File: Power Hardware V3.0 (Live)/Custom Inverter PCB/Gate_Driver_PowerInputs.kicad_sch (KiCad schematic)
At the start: 22 parts, among them J1 1714971, J2 1714971, J3 1714968, J7 1714971, J8 1714971, K2 1-1393210-3, U1 DRV8300DIPWR

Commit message: Datasheets into components
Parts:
- CR4: Part Number (none) -> LD1085D2M33R
- K2: Part Number (none) -> 1-1393210-3
- U1: Part Number (none) -> DRV8300DIPWR
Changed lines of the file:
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@@
 			)
 		)
-		(property "Datasheet" "DRV8300DIPWR"
+		(property "Datasheet" "https://www.ti.com/lit/ds/symlink/drv8300.pdf"
 			(at 173.99 30.48 0)
 			(effects
@@
 			)
 		)
-		(property "Description" ""
+		(property "Description" "IC GATE DRV HI/LOW SIDE 20HTSSOP"
 			(at 173.99 30.48 0)
 			(effects
@@
 			)
 		)
-		(property "Part Number" ""
+		(property "Part Number" "DRV8300DIPWR"
 			(at 173.99 30.48 0)
 			(effects
@@
 			)
 		)
-		(property "Datasheet" "LD1085D2M33R"
+		(property "Datasheet" "https://www.st.com/content/ccc/resource/technical/document/datasheet/d3/84/d5/f6/3c/23/40/7b/CD00001883.pdf/files/CD00001883.pdf/jcr:content/translations/en.CD00001883.pdf"
 			(at 133.35 147.32 0)
 			(effects
@@
 			)
 		)
-		(property "Description" ""
+		(property "Description" "IC REG LINEAR 3.3V 3A D2PAK-3"
+			(at 133.35 147.32 0)
+			(effects
+				(font
+					(size 1.27 1.27)
+				)
+				(hide yes)
+			)
+		)
+		(property "Part Number" "LD1085D2M33R"
 			(at 133.35 147.32 0)
 			(effects
@@
 			)
 		)
-		(property "Datasheet" ""
+		(property "Datasheet" "https://www.te.com/en/product-1-1393210-3.datasheet.pdf"
 			(at 123.19 67.31 0)
 			(effects
@@
 			)
 		)
-		(property "Description" ""
+		(property "Description" "General Purpose Power Relay, DC, Monostable, 1 Form A SPST-NO, 30 A Contact Rating, 12 VDC Coil Voltage, Potter & Brumfield T9A"
 			(at 123.19 67.31 0)
 			(effects
@@
 			)
 		)
-		(property "Part Number" ""
+		(property "Part Number" "1-1393210-3"
 			(at 123.19 67.31 0)
 			(effects

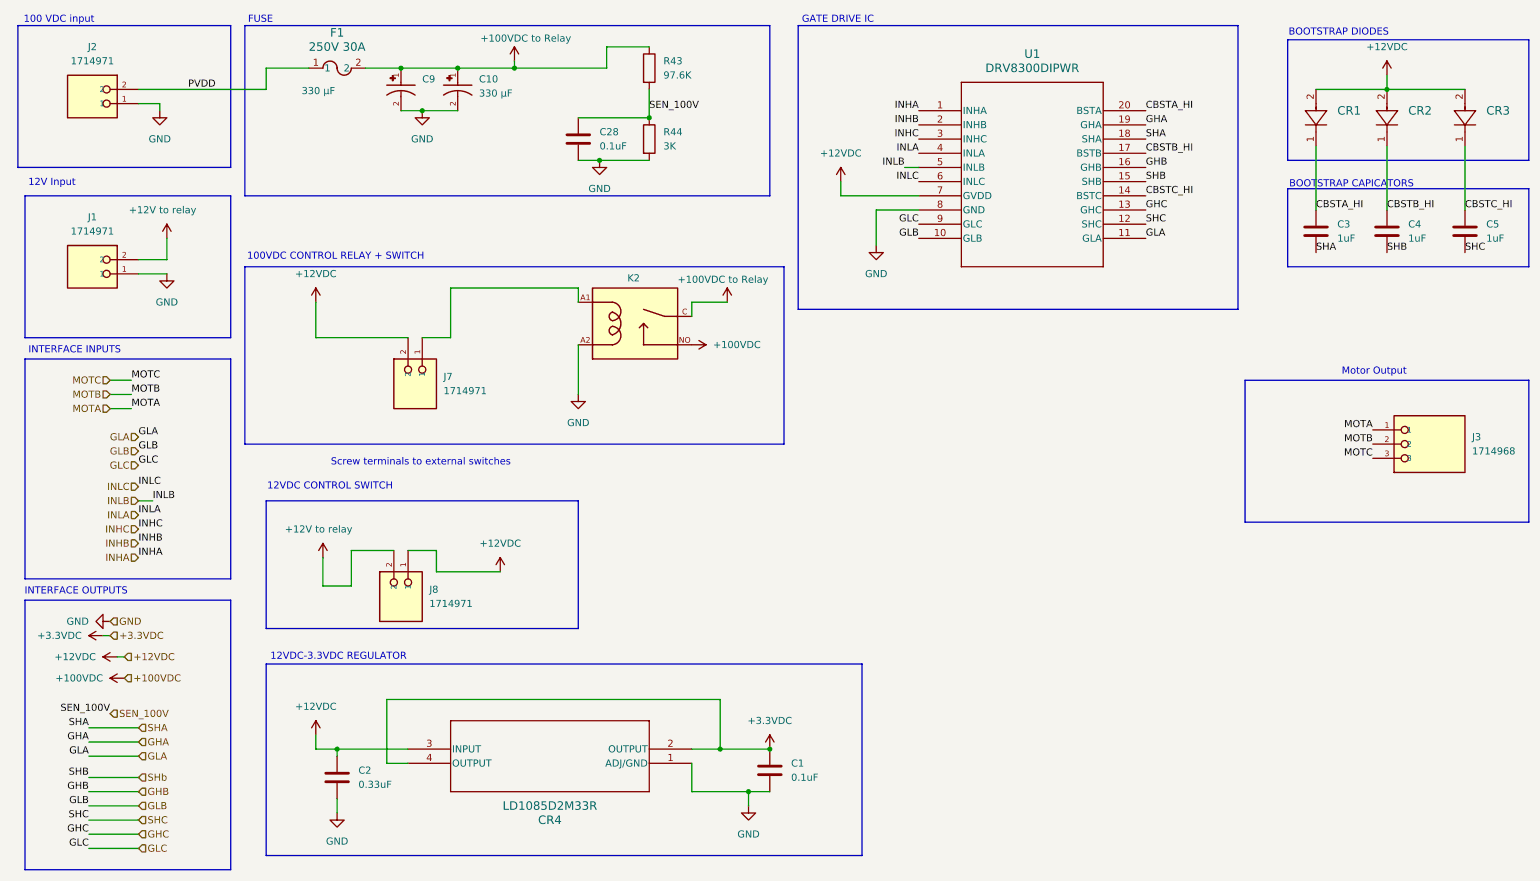
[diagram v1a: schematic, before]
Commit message: Added 100-12 and 12-5 regulators added fan headers
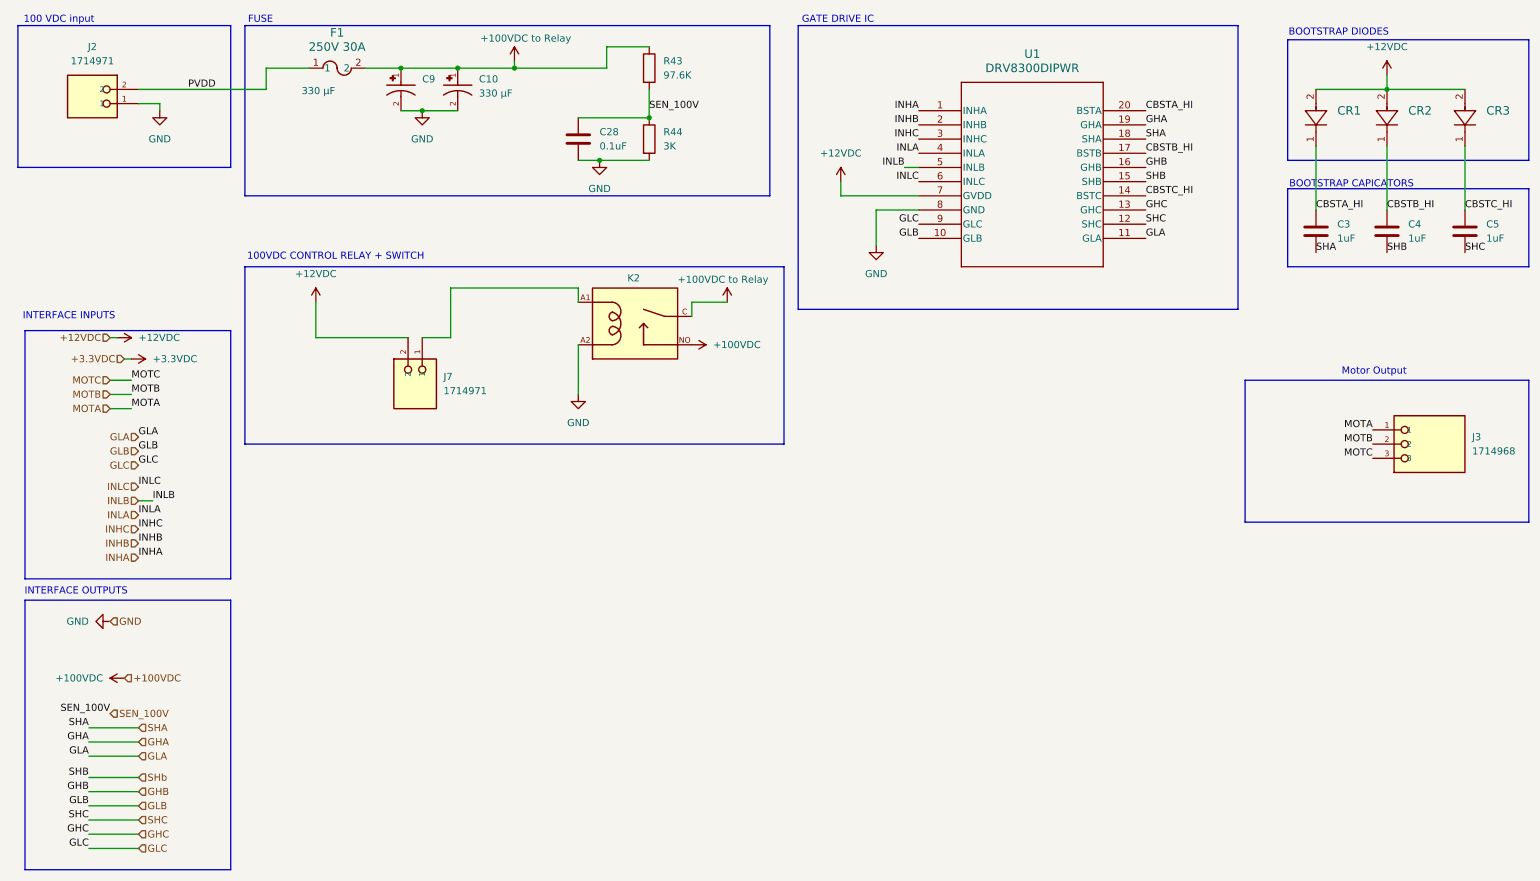
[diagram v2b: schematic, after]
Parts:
- removed C1: 0.1uF, Capacitor_SMD:C_0805_2012Metric, symbol Device:C
- removed C2: 0.33uF, Capacitor_SMD:C_0805_2012Metric, symbol Device:C
- removed CR4: LD1085D2M33R, LD1085D2M33R:D2PAK&slash_A_STM, symbol 3.3V Regulator:LD1085D2M33R
- removed J1, J8: 1714971, 1714971:PHOENIX_1714971, symbol 1714971:1714971
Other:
- note removed: "12V Input"
- note removed: "12VDC CONTROL SWITCH"
- note removed: "12VDC-3.3VDC REGULATOR"
- note removed: "Screw terminals to external switches"

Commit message: Fixes
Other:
- moved on the sheet: J7, K2

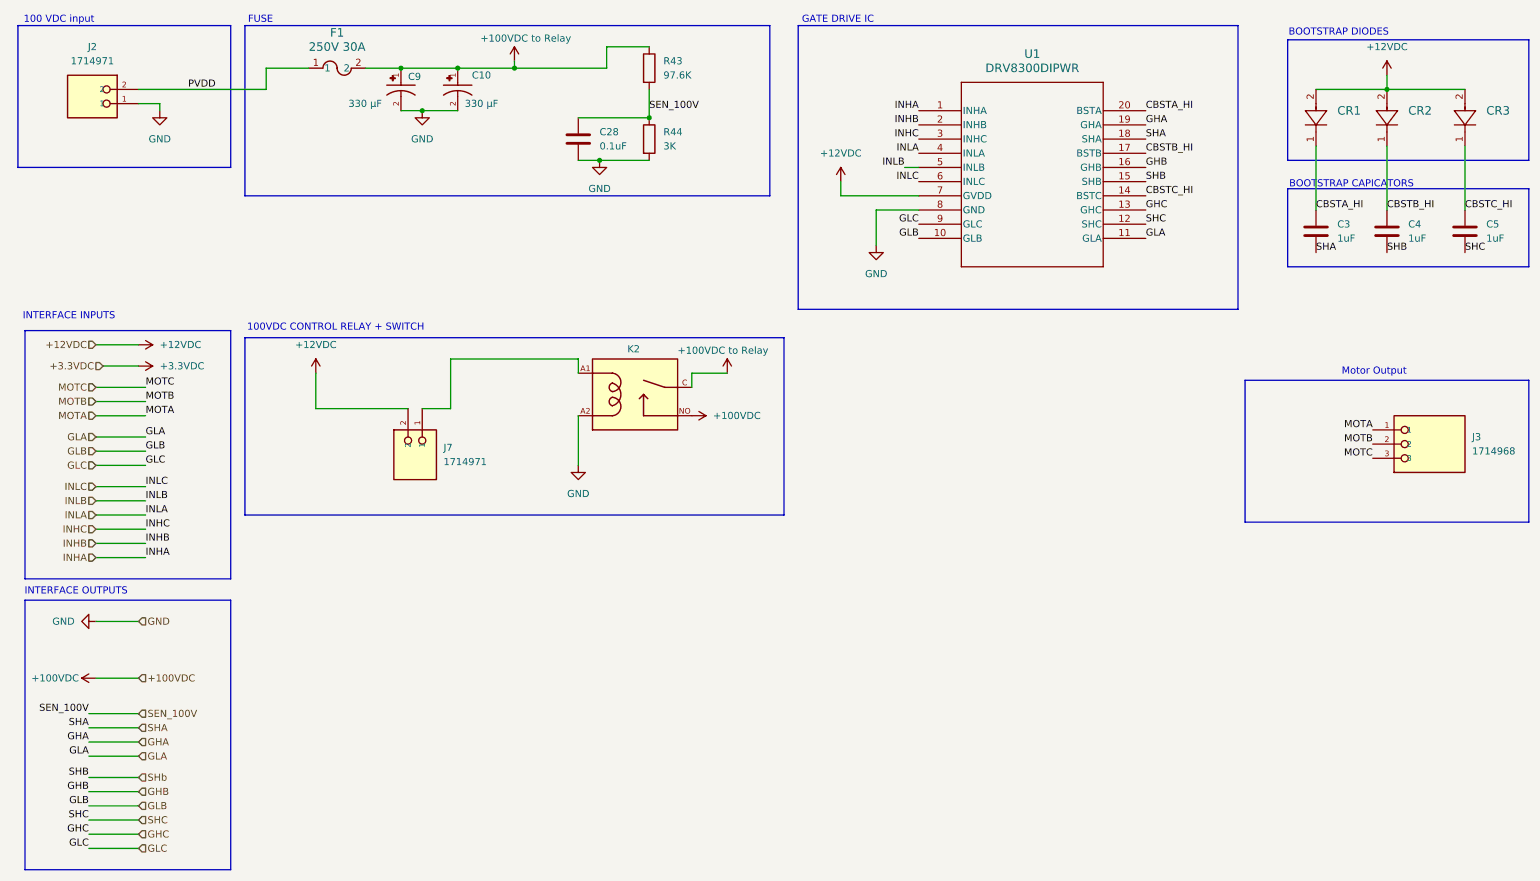
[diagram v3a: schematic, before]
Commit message: PCB V3 changes
-HV outputs and inputs changed to screw terminals for lugs
- Fuses changes to 50A
- ADC pin for temp sense along with the temp sensing circuit
- Added more pins to motor encoder term for temp sense
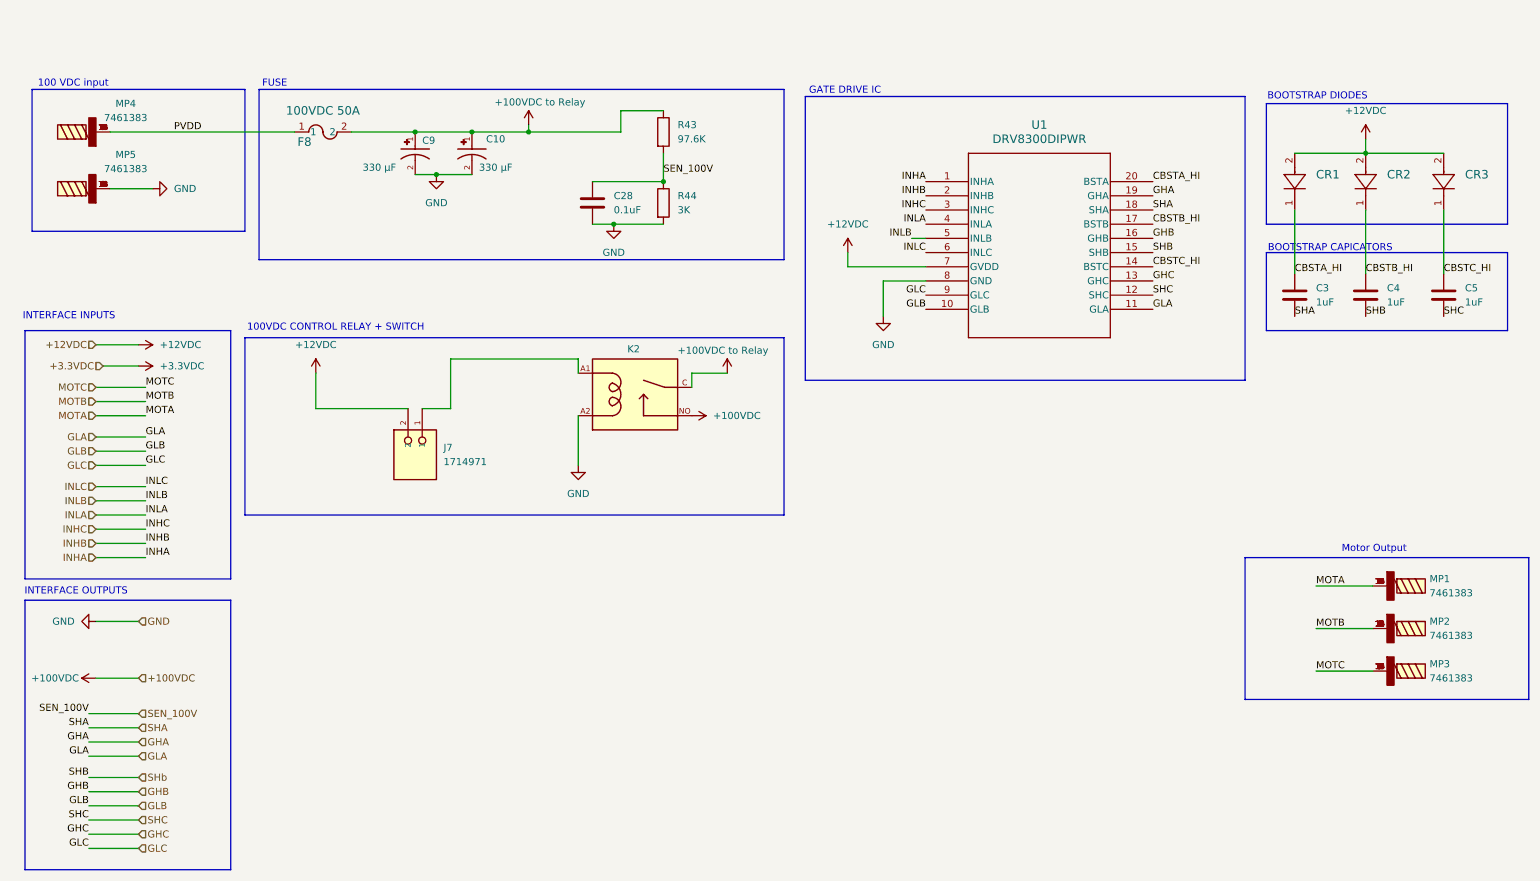
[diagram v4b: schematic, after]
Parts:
- removed F1: 250V 30A, 0463030_ER:FUSE_0463_LTF-M, symbol 2025-02-24_21-09-15:0463030.ER
- removed J2: 1714971, 1714971:PHOENIX_1714971, symbol 1714971:1714971
- removed J3: 1714968, PHOENIX_1714968:PHOENIX_1714968, symbol 1714968:1714968
- added F8: 100VDC 50A, 0463030_ER:FUSE_0463_LTF-M, symbol 2025-02-24_21-09-15:0463030.ER
- added MP1, MP2, MP3, MP4, MP5: 7461383, M5 Screw Term 7461383:WP-SHFU_7461383, symbol M5 Screw Terminal 7461383:WP-SHFU
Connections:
- net +100VDC to Relay: now also F8.2
- net GND: now also MP5.1, MP5.10, MP5.11, MP5.12, MP5.13, MP5.14, MP5.15, MP5.16, MP5.2, MP5.3, MP5.4, MP5.5, MP5.6, MP5.7, MP5.8, MP5.9
- net MOTA: now also MP1.1, MP1.10, MP1.11, MP1.12, MP1.13, MP1.14, MP1.15, MP1.16, MP1.2, MP1.3, MP1.4, MP1.5, MP1.6, MP1.7, MP1.8, MP1.9
- net MOTB: now also MP2.1, MP2.10, MP2.11, MP2.12, MP2.13, MP2.14, MP2.15, MP2.16, MP2.2, MP2.3, MP2.4, MP2.5, MP2.6, MP2.7, MP2.8, MP2.9
- net MOTC: now also MP3.1, MP3.10, MP3.11, MP3.12, MP3.13, MP3.14, MP3.15, MP3.16, MP3.2, MP3.3, MP3.4, MP3.5, MP3.6, MP3.7, MP3.8, MP3.9
- net PVDD: now also F8.1, MP4.1, MP4.10, MP4.11, MP4.12, MP4.13, MP4.14, MP4.15, MP4.16, MP4.2, MP4.3, MP4.4, MP4.5, MP4.6, MP4.7, MP4.8, MP4.9
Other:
- moved on the sheet: C10, C28, C3, C4, C5, C9, CR1, CR2, CR3, R43, R44, U1

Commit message: PCB layout
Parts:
- removed J7: 1714971, 1714971:PHOENIX_1714971, symbol 1714971:1714971
- added J1: 1990009, 2P term 1990009:PHOENIX_1990009, symbol 1990009 2P term:1990009
- renumbered C9 to C1, C10 to C2, C28 to C3, C3 to C4, C4 to C5, C5 to C6, F8 to F1, K2 to K1, MP4 to MP1, MP5 to MP2, MP1 to MP3, MP2 to MP4, MP3 to MP5, R43 to R1, R44 to R2
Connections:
- net +12VDC: now also J1.2
- net at K1.A1: now also J1.1

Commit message: V3.0 is ordered
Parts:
- added D10: BRIDGE ON, Capacitor_SMD:C_0603_1608Metric_Pad1.08x0.95mm_HandSolder, symbol Device:LED
- added D11: 100V IN, Capacitor_SMD:C_0603_1608Metric_Pad1.08x0.95mm_HandSolder, symbol Device:LED
- added R49, R50, R51, R52: 2.7k, Resistor_SMD:R_0805_2012Metric, symbol Device:R
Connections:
- net +100VDC: now also R49.2
- net +100VDC to Relay: now also R51.2
- net GND: now also D10.1 (K), D11.1 (K)
- new net: D10.2 (A), R50.1
- new net: R51.1, R52.2
- new net: R49.1, R50.2
- new net: D11.2 (A), R52.1
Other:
- note added: "100V BRIDGE ACTIVE LIGHT"
- note added: "100V INPUT ACTIVE LIGHT"

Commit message: V3 push
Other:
- moved on the sheet: J1
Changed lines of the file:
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@@
 	(wire
 		(pts
-			(xy 85.09 83.82) (xy 90.17 83.82)
-		)
-		(stroke
-			(width 0)
-			(type default)
-		)
-	)
-	(wire
-		(pts
 			(xy 172.72 50.8) (xy 175.26 50.8)
 		)
@@
 	(wire
 		(pts
-			(xy 90.17 83.82) (xy 90.17 74.93)
-		)
-		(stroke
-			(width 0)
-			(type default)
-		)
-	)
-	(wire
-		(pts
 			(xy 88.9 143.51) (xy 90.17 143.51)
 		)
@@
 	(wire
 		(pts
-			(xy 66.04 83.82) (xy 82.55 83.82)
+			(xy 76.2 77.47) (xy 91.44 77.47)
 		)
 		(stroke
@@
 	(wire
 		(pts
-			(xy 66.04 77.47) (xy 66.04 83.82)
-		)
-		(stroke
-			(width 0)
-			(type default)
-		)
-	)
-	(wire
-		(pts
 			(xy 241.3 48.26) (xy 241.3 59.69)
 		)
@@
 	(wire
 		(pts
-			(xy 90.17 74.93) (xy 113.03 74.93)
+			(xy 93.98 77.47) (xy 113.03 77.47)
 		)
 		(stroke
@@
 	(wire
 		(pts
-			(xy 113.03 74.93) (xy 113.03 77.47)
-		)
-		(stroke
-			(width 0)
-			(type default)
-		)
-	)
-	(wire
-		(pts
 			(xy 120.65 34.29) (xy 104.14 34.29)
 		)
@@
 	(symbol
 		(lib_id "1990009 2P term:1990009")
-		(at 85.09 91.44 270)
+		(at 93.98 85.09 270)
 		(unit 1)
 		(exclude_from_sim no)
@@
 		(fields_autoplaced yes)
 		(property "Reference" "J1"
-			(at 88.9 90.8049 90)
+			(at 97.79 84.4549 90)
 			(effects
 				(font
@@
 		)
 		(property "Value" "1990009"
-			(at 88.9 93.3449 90)
+			(at 97.79 86.9949 90)
 			(effects
 				(font
@@
 		)
 		(property "Footprint" "2P term 1990009:PHOENIX_1990009"
-			(at 85.09 91.44 0)
+			(at 93.98 85.09 0)
 			(effects
 				(font
@@
 		)
 		(property "Datasheet" ""
-			(at 85.09 91.44 0)
+			(at 93.98 85.09 0)
 			(effects
 				(font
@@
 		)
 		(property "Description" ""
-			(at 85.09 91.44 0)
+			(at 93.98 85.09 0)
 			(effects
 				(font
@@
 		)
 		(property "PARTREV" "03.02.2023"
-			(at 85.09 91.44 0)
+			(at 93.98 85.09 0)
 			(effects
 				(font
@@
 		)
 		(property "STANDARD" "Manufacturer Recommendations"
-			(at 85.09 91.44 0)
+			(at 93.98 85.09 0)
 			(effects
 				(font
@@
 		)
 		(property "MAXIMUM_PACKAGE_HEIGHT" "13.1mm"
-			(at 85.09 91.44 0)
+			(at 93.98 85.09 0)
 			(effects
 				(font
@@
 		)
 		(property "MANUFACTURER" "Phoenix Contact"
-			(at 85.09 91.44 0)
+			(at 93.98 85.09 0)
 			(effects
 				(font
@@
 	(symbol
 		(lib_id "power:+12V")
-		(at 66.04 77.47 0)
+		(at 76.2 77.47 90)
 		(unit 1)
 		(exclude_from_sim no)
@@
 		(fields_autoplaced yes)
 		(property "Reference" "#PWR06"
-			(at 66.04 81.28 0)
+			(at 80.01 77.47 0)
 			(effects
 				(font
@@
 		)
 		(property "Value" "+12VDC"
-			(at 66.04 72.39 0)
+			(at 72.39 77.4699 90)
 			(effects
 				(font
 					(size 1.27 1.27)
 				)
+				(justify left)
 			)
 		)
 		(property "Footprint" ""
-			(at 66.04 77.47 0)
+			(at 76.2 77.47 0)
 			(effects
 				(font
@@
 		)
 		(property "Datasheet" ""
-			(at 66.04 77.47 0)
+			(at 76.2 77.47 0)
 			(effects
 				(font
@@
 		)
 		(property "Description" "Power symbol creates a global label with name \"+12V\""
-			(at 66.04 77.47 0)
+			(at 76.2 77.47 0)
 			(effects
 				(font

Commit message: changes
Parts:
- J1: Part Number (none) -> 1990009
- MP1, MP2, MP3, MP4, MP5: Part Number (none) -> 7461383
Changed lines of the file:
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@@
+			)
+		)
+		(property "Part Number" "7461383"
+			(at 24.13 44.45 90)
+			(effects
+				(font
+					(size 1.27 1.27)
+				)
+				(hide yes)
 			)
 		)
@@
 			)
 		)
+		(property "Part Number" "1990009"
+			(at 93.98 85.09 90)
+			(effects
+				(font
+					(size 1.27 1.27)
+				)
+				(hide yes)
+			)
+		)
 		(pin "1"
 		)
@@
 			)
 		)
+		(property "Part Number" "7461383"
+			(at 260.35 130.81 90)
+			(effects
+				(font
+					(size 1.27 1.27)
+				)
+				(hide yes)
+			)
+		)
 		(pin "5"
 		)
@@
 			)
 		)
+		(property "Part Number" "7461383"
+			(at 260.35 123.19 90)
+			(effects
+				(font
+					(size 1.27 1.27)
+				)
+				(hide yes)
+			)
+		)
 		(pin "5"
 		)
@@
 			)
 		)
+		(property "Part Number" "7461383"
+			(at 24.13 34.29 90)
+			(effects
+				(font
+					(size 1.27 1.27)
+				)
+				(hide yes)
+			)
+		)
 		(pin "5"
 		)
@@
 			(effects
 				(font
+					(size 1.27 1.27)
+				)
+				(hide yes)
+			)
+		)
+		(property "Part Number" "7461383"
+			(at 260.35 115.57 90)
+			(effects
+				(font
